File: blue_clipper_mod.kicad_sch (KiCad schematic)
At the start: 8 parts

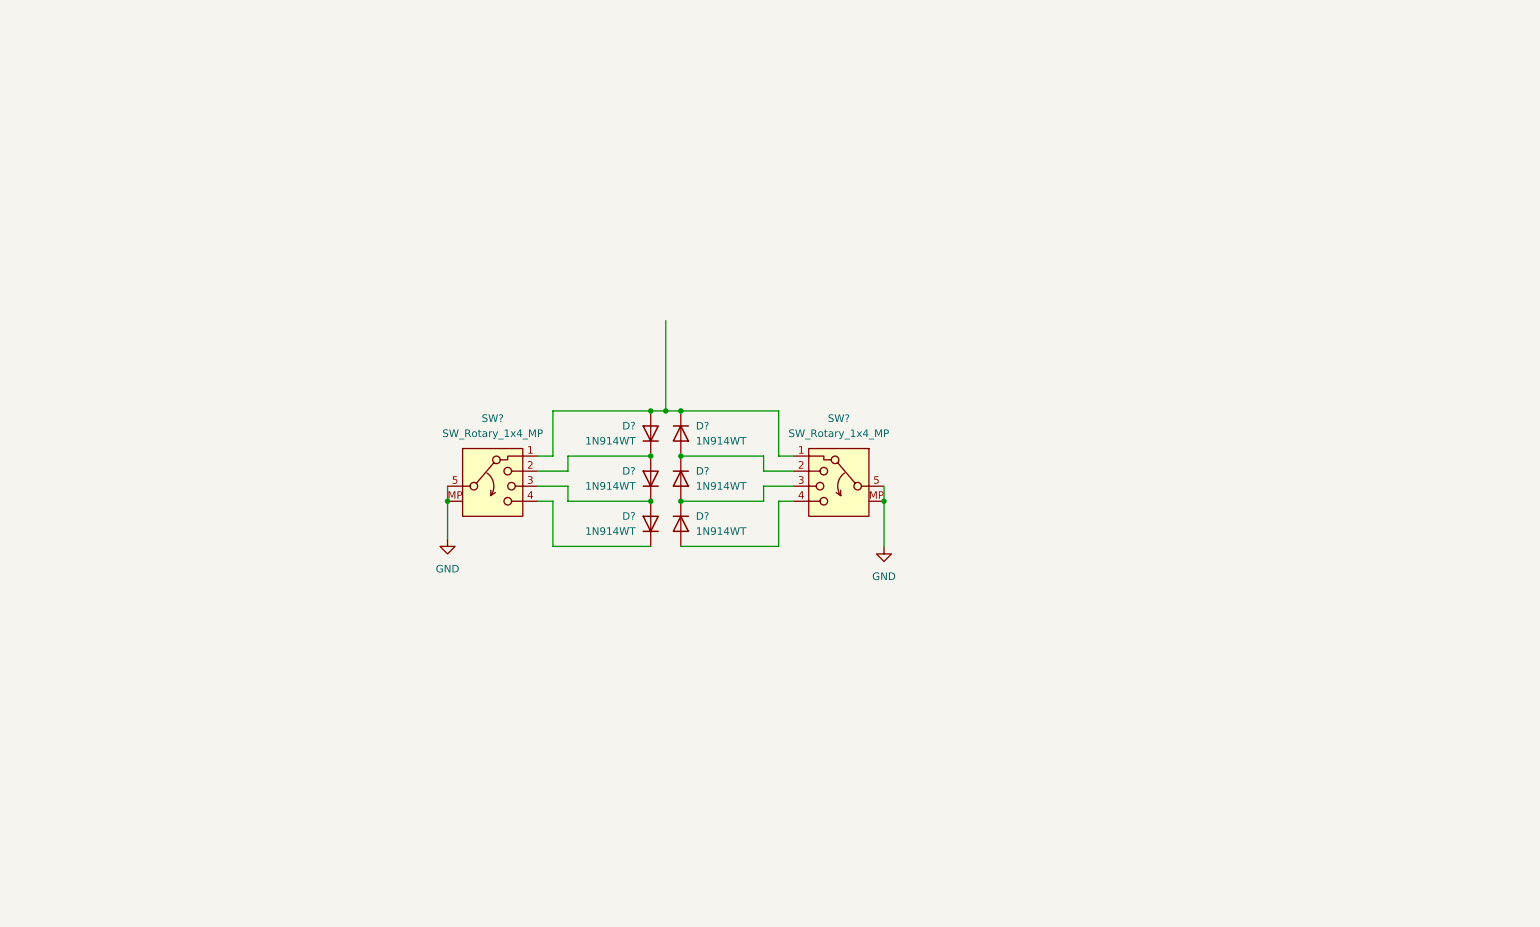
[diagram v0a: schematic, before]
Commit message: Clean Up schematic
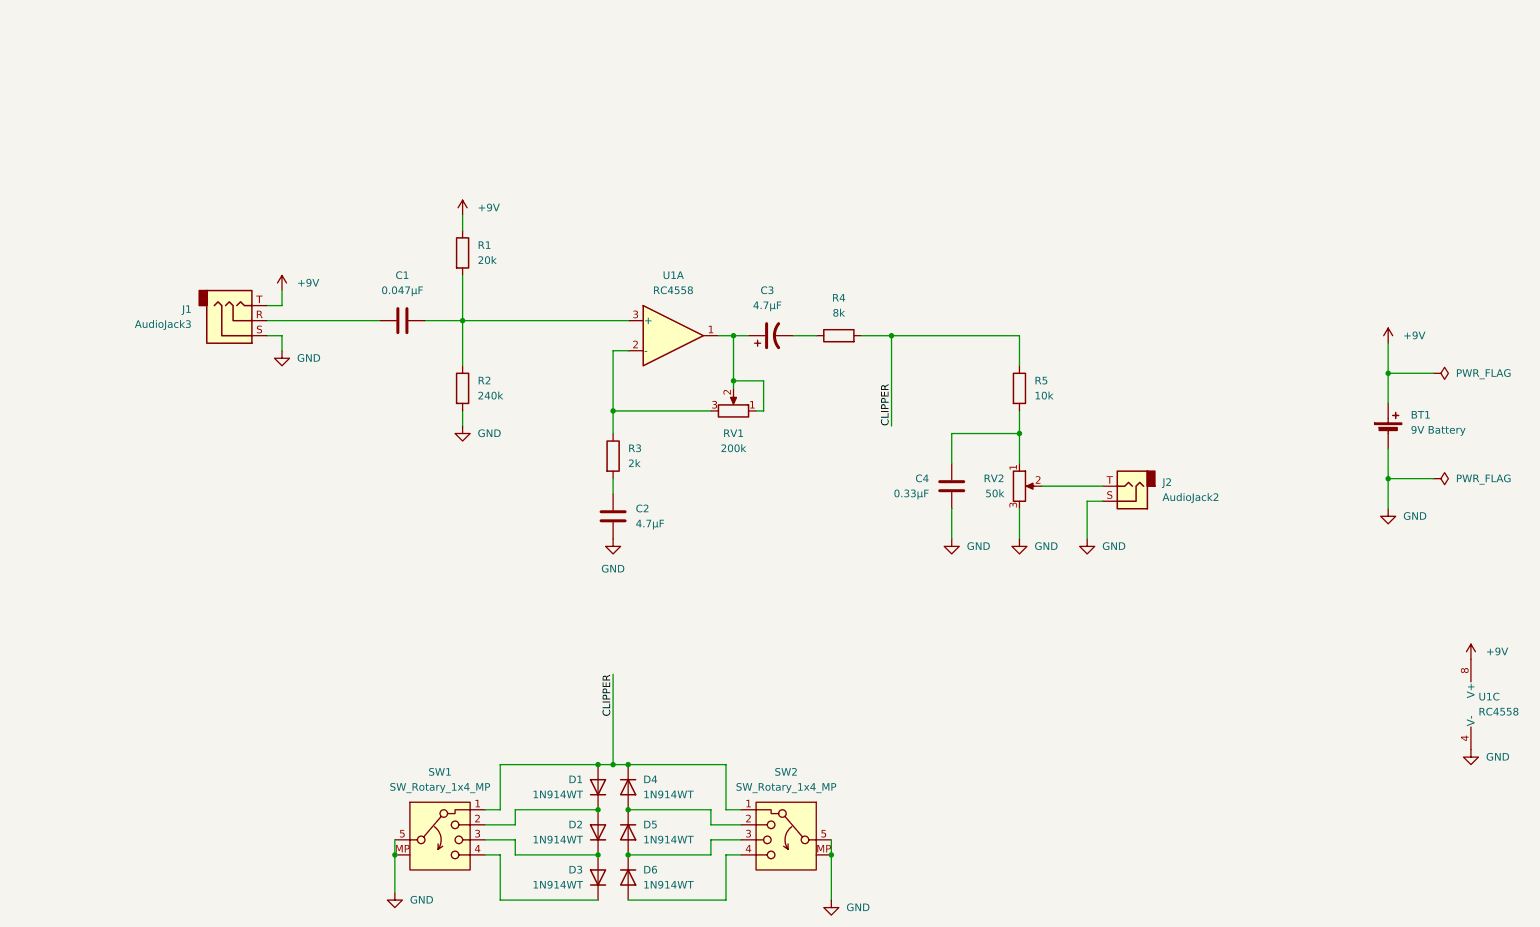
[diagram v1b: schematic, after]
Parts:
- added BT1: 9V Battery, symbol Device:Battery_Cell
- added C1: 0.047µF, symbol Device:C
- added C2: 4.7µF, symbol Device:C
- added C3: 4.7µF, symbol Device:C_Polarized_US
- added C4: 0.33µF, symbol Device:C
- added J1: AudioJack3, symbol Connector_Audio:AudioJack3
- added J2: AudioJack2, symbol Connector_Audio:AudioJack2
- added R1: 20k, symbol Device:R
- added R2: 240k, symbol Device:R
- added R3: 2k, symbol Device:R
- added R4: 8k, symbol Device:R
- added R5: 10k, symbol Device:R
- added RV1: 200k, symbol Device:R_Potentiometer
- added RV2: 50k, symbol Device:R_Potentiometer
- added U1: RC4558, symbol Amplifier_Operational:RC4558
- gave numbers to parts that had none: 8
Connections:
- net GND: now also BT1.2 (-), C2.2, C4.2, J1.S, J2.S, R2.2, RV2.3, U1.4 (V-)
- net CLIPPER: now reaches D1.2 (A), D4.1 (K), SW1.1, SW2.1
- net CLIPPER: now also R4.2, R5.1
- new net: C1.2, R1.2, R2.1, U1.3 (+)
- new net: C4.1, R5.2, RV2.1
- new net: J2.T, RV2.2
- new net: C3.1, RV1.1, RV1.2, U1.1
- new net: R3.1, RV1.3, U1.2 (-)
- new net: C2.1, R3.2
- new net: C3.2, R4.1
- new net: C1.1, J1.R
- new net +9V: BT1.1 (+), J1.T, R1.1, U1.8 (V+)
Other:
- moved on the sheet: D1, D2, D3, D4, D5, D6, SW1, SW2

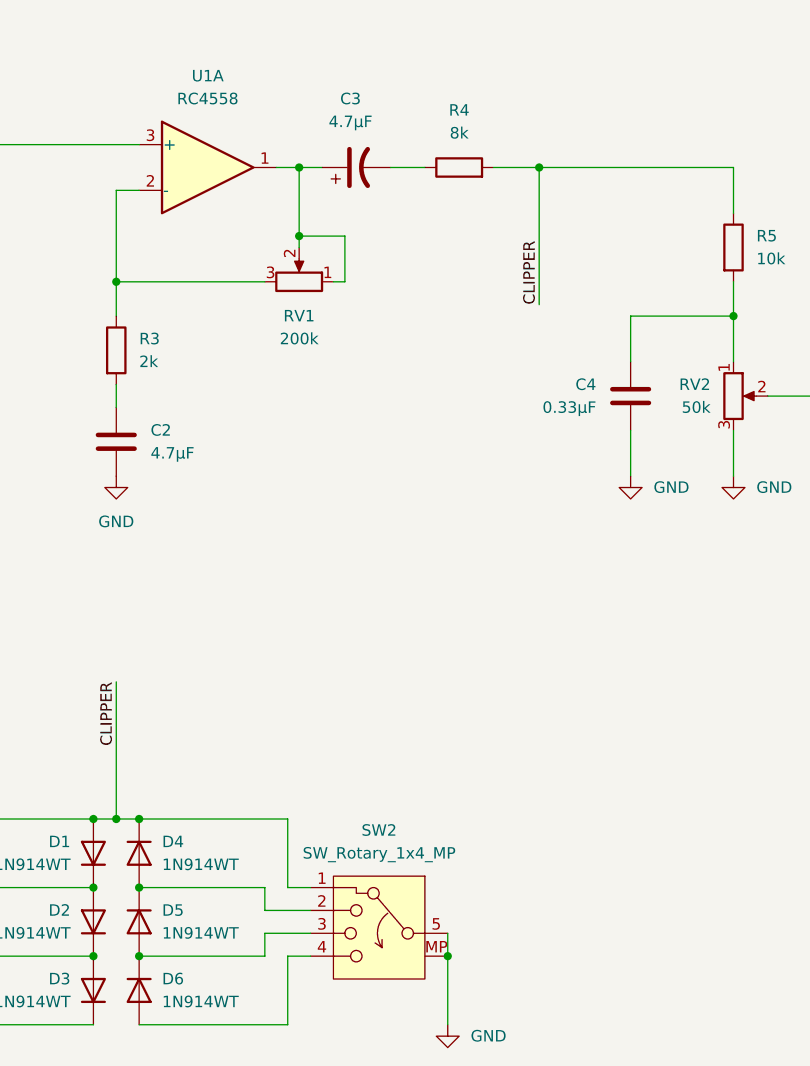
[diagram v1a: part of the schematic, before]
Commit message: schematic probably good - round tracks fully necessary
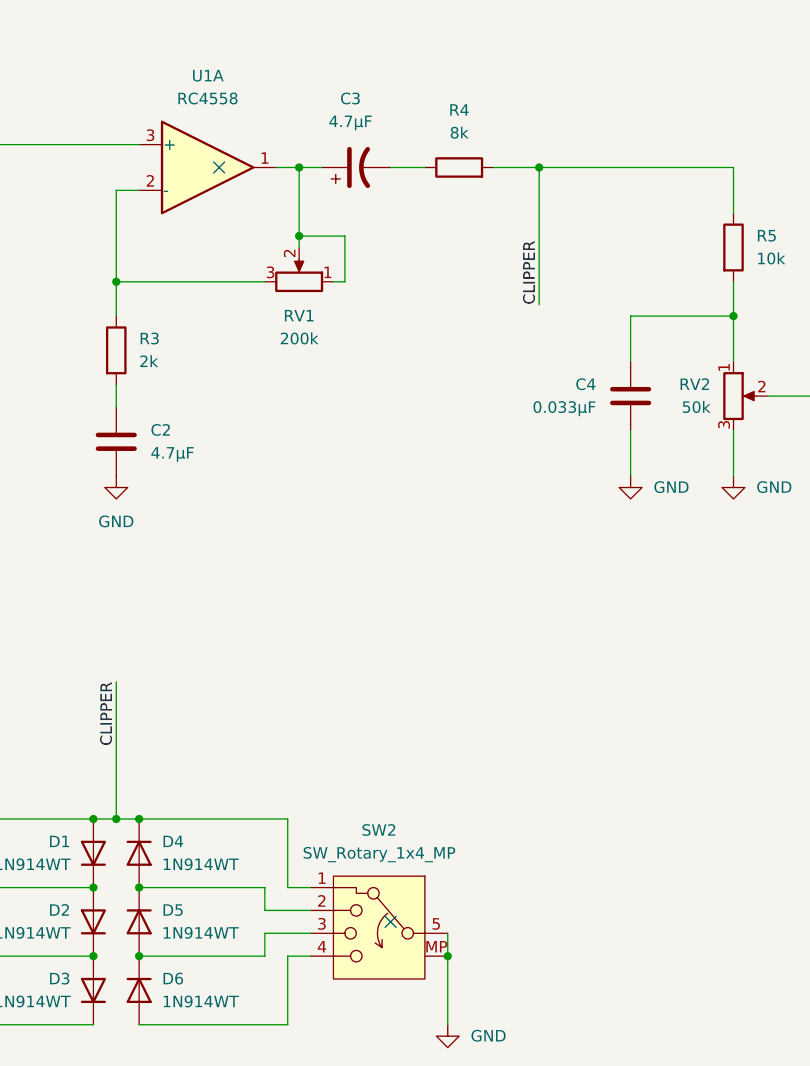
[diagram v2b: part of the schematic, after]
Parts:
- BT1: footprint (none) -> Battery:BatteryHolder_MPD_BA9VPC_1xPP3
- C1: footprint (none) -> Capacitor_THT:CP_Radial_Tantal_D6.0mm_P5.00mm
- C2: footprint (none) -> Capacitor_THT:CP_Radial_D22.0mm_P10.00mm_SnapIn
- C3: footprint (none) -> Capacitor_THT:CP_Radial_D26.0mm_P10.00mm_SnapIn
- C4: value 0.33µF -> 0.033µF; footprint (none) -> Capacitor_THT:C_Disc_D8.0mm_W5.0mm_P10.00mm
- J1, J2: footprint (none) -> Connector_Audio:Jack_3.5mm_CUI_SJ-3523-SMT_Horizontal
- R1, R2, R3, R4, R5: footprint (none) -> Resistor_THT:R_Axial_DIN0614_L14.3mm_D5.7mm_P5.08mm_Vertical
- RV1, RV2: footprint (none) -> Potentiometer_THT:Potentiometer_Piher_PC-16_Single_Vertical
- SW1, SW2: footprint (none) -> Rotary_Encoder:RotaryEncoder_Alps_EC12E-Switch_Vertical_H20mm_CircularMountingHoles
- U1: footprint (none) -> Package_DIP:DIP-8_W10.16mm
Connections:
- no-connect marks 0 -> 2
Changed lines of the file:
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@@
   (junction (at 193.04 100.33) (diameter 0) (color 0 0 0 0)
   )
+  (no_connect (at 135.89 83.82))
+  (no_connect (at 154.94 167.64))
   (wire (pts (xy 124.46 96.52) (xy 124.46 100.33))
     (stroke (width 0) (type default))
@@
       (effects (font (size 1.27 1.27)) (justify left))
     )
-    (property "Footprint" "" (at 97.282 69.85 90)
+    (property "Footprint" "Resistor_THT:R_Axial_DIN0614_L14.3mm_D5.7mm_P5.08mm_Vertical" (at 97.282 69.85 90)
       (effects (font (size 1.27 1.27)) hide)
     )
@@
       (effects (font (size 1.27 1.27)))
     )
-    (property "Footprint" "" (at 95.25 179.07 0)
+    (property "Footprint" "Rotary_Encoder:RotaryEncoder_Alps_EC12E-Switch_Vertical_H20mm_CircularMountingHoles" (at 95.25 179.07 0)
       (effects (font (size 1.27 1.27)) hide)
     )
@@
       (effects (font (size 1.27 1.27)) (justify right))
     )
-    (property "Footprint" "" (at 193.04 109.22 0)
+    (property "Footprint" "Potentiometer_THT:Potentiometer_Piher_PC-16_Single_Vertical" (at 193.04 109.22 0)
       (effects (font (size 1.27 1.27)) hide)
     )
@@
       (effects (font (size 1.27 1.27)) (justify right))
     )
-    (property "Value" "0.33µF" (at 177.8 110.49 0)
+    (property "Value" "0.033µF" (at 177.8 110.49 0)
       (effects (font (size 1.27 1.27)) (justify right))
     )
-    (property "Footprint" "" (at 182.5752 113.03 0)
+    (property "Footprint" "Capacitor_THT:C_Disc_D8.0mm_W5.0mm_P10.00mm" (at 182.5752 113.03 0)
       (effects (font (size 1.27 1.27)) hide)
     )
@@
       (effects (font (size 1.27 1.27)) (justify left))
     )
-    (property "Footprint" "" (at 191.262 92.71 90)
+    (property "Footprint" "Resistor_THT:R_Axial_DIN0614_L14.3mm_D5.7mm_P5.08mm_Vertical" (at 191.262 92.71 90)
       (effects (font (size 1.27 1.27)) hide)
     )
@@
       (effects (font (size 1.27 1.27)))
     )
-    (property "Footprint" "" (at 144.78 96.52 0)
+    (property "Footprint" "Potentiometer_THT:Potentiometer_Piher_PC-16_Single_Vertical" (at 144.78 96.52 0)
       (effects (font (size 1.27 1.27)) hide)
     )
@@
       (effects (font (size 1.27 1.27)) (justify left))
     )
-    (property "Footprint" "" (at 122.682 104.14 90)
+    (property "Footprint" "Resistor_THT:R_Axial_DIN0614_L14.3mm_D5.7mm_P5.08mm_Vertical" (at 122.682 104.14 90)
       (effects (font (size 1.27 1.27)) hide)
     )
@@
       (effects (font (size 1.27 1.27)))
     )
-    (property "Footprint" "" (at 134.62 83.82 0)
+    (property "Footprint" "Package_DIP:DIP-8_W10.16mm" (at 134.62 83.82 0)
       (effects (font (size 1.27 1.27)) hide)
     )
@@
       (effects (font (size 1.27 1.27)) (justify left))
     )
-    (property "Footprint" "" (at 125.4252 118.11 0)
+    (property "Footprint" "Capacitor_THT:CP_Radial_D22.0mm_P10.00mm_SnapIn" (at 125.4252 118.11 0)
       (effects (font (size 1.27 1.27)) hide)
     )
@@
       (effects (font (size 1.27 1.27)))
     )
-    (property "Footprint" "" (at 162.56 85.598 90)
+    (property "Footprint" "Resistor_THT:R_Axial_DIN0614_L14.3mm_D5.7mm_P5.08mm_Vertical" (at 162.56 85.598 90)
       (effects (font (size 1.27 1.27)) hide)
     )
@@
       (effects (font (size 1.27 1.27)) (justify left))
     )
-    (property "Footprint" "" (at 271.78 146.05 0)
+    (property "Footprint" "Package_DIP:DIP-8_W10.16mm" (at 271.78 146.05 0)
       (effects (font (size 1.27 1.27)) hide)
     )
@@
       (effects (font (size 1.27 1.27)))
     )
-    (property "Footprint" "" (at 153.67 179.07 0)
+    (property "Footprint" "Rotary_Encoder:RotaryEncoder_Alps_EC12E-Switch_Vertical_H20mm_CircularMountingHoles" (at 153.67 179.07 0)
       (effects (font (size 1.27 1.27)) hide)
     )
@@
       (effects (font (size 1.27 1.27)) (justify left))
     )
-    (property "Footprint" "" (at 255.27 98.806 90)
+    (property "Footprint" "Battery:BatteryHolder_MPD_BA9VPC_1xPP3" (at 255.27 98.806 90)
       (effects (font (size 1.27 1.27)) hide)
     )
@@
       (effects (font (size 1.27 1.27)) (justify right))
     )
-    (property "Footprint" "" (at 212.09 109.22 0)
+    (property "Footprint" "Connector_Audio:Jack_3.5mm_CUI_SJ-3523-SMT_Horizontal" (at 212.09 109.22 0)
       (effects (font (size 1.27 1.27)) hide)
     )
@@
       (effects (font (size 1.27 1.27)) (justify left))
     )
-    (property "Footprint" "" (at 97.282 92.71 90)
+    (property "Footprint" "Resistor_THT:R_Axial_DIN0614_L14.3mm_D5.7mm_P5.08mm_Vertical" (at 97.282 92.71 90)
       (effects (font (size 1.27 1.27)) hide)
     )
@@
       (effects (font (size 1.27 1.27)) (justify right))
     )
-    (property "Footprint" "" (at 60.96 81.28 0)
+    (property "Footprint" "Connector_Audio:Jack_3.5mm_CUI_SJ-3523-SMT_Horizontal" (at 60.96 81.28 0)
       (effects (font (size 1.27 1.27)) hide)
     )
@@
       (effects (font (size 1.27 1.27)))
     )
-    (property "Footprint" "" (at 92.71 80.3148 0)
+    (property "Footprint" "Capacitor_THT:CP_Radial_Tantal_D6.0mm_P5.00mm" (at 92.71 80.3148 0)
       (effects (font (size 1.27 1.27)) hide)
     )
@@
       (effects (font (size 1.27 1.27)))
     )
-    (property "Footprint" "" (at 151.13 83.82 0)
-      (effects (font (size 1.27 1.27)) hide)
-    )
+    (property "Footprint" "Capacitor_THT:CP_Radial_D26.0mm_P10.00mm_SnapIn" (at 151.13 83.82 0)
+      (effects (font (size 1.27 1.27)) hide)
+    )

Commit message: fix everything
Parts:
- removed C3: 4.7µF, Capacitor_THT:CP_Radial_D26.0mm_P10.00mm_SnapIn, symbol Device:C_Polarized_US
- removed J1: AudioJack3, Connector_Audio:Jack_3.5mm_CUI_SJ-3523-SMT_Horizontal, symbol Connector_Audio:AudioJack3
- removed J2: AudioJack2, Connector_Audio:Jack_3.5mm_CUI_SJ-3523-SMT_Horizontal, symbol Connector_Audio:AudioJack2
- removed SW1, SW2: SW_Rotary_1x4_MP, Rotary_Encoder:RotaryEncoder_Alps_EC12E-Switch_Vertical_H20mm_CircularMountingHoles, symbol Switch:SW_Rotary_1x4_MP
- added C3: 4.7µF, Capacitor_THT:CP_Radial_D4.0mm_P1.50mm, symbol Device:C
- added H1, H2, H3, H4: MountingHole, MountingHole:MountingHole_3.2mm_M3, symbol Mechanical:MountingHole
- added J1: IN, custom:jack_pads, symbol Connector_Audio:AudioJack2_SwitchT
- added J2: OUT, custom:jack_pads, symbol Connector_Audio:AudioJack2_SwitchT
- added JP1, JP2: SolderJumper_2_Open, Jumper:SolderJumper-2_P1.3mm_Open_RoundedPad1.0x1.5mm, symbol Jumper:SolderJumper_2_Open
- added R6, R7: 50k, Resistor_SMD:R_0603_1608Metric_Pad0.98x0.95mm_HandSolder, symbol Device:R
- added SW1, SW2: ~, Connector_PinHeader_2.54mm:PinHeader_1x05_P2.54mm_Vertical, symbol custom:SP4T
- added SW3: BYPASS, Connector_PinHeader_2.54mm:PinHeader_1x06_P2.54mm_Vertical, symbol Switch:SW_Push_DPDT
- added unit 2 of U1
- BT1: footprint Battery:BatteryHolder_MPD_BA9VPC_1xPP3 -> Connector_PinHeader_2.54mm:PinHeader_1x02_P2.54mm_Vertical
- C1: footprint Capacitor_THT:CP_Radial_Tantal_D6.0mm_P5.00mm -> Capacitor_SMD:C_0603_1608Metric
- C2: footprint Capacitor_THT:CP_Radial_D22.0mm_P10.00mm_SnapIn -> Capacitor_THT:CP_Radial_D4.0mm_P1.50mm
- C4: footprint Capacitor_THT:C_Disc_D8.0mm_W5.0mm_P10.00mm -> Capacitor_SMD:C_0603_1608Metric_Pad1.08x0.95mm_HandSolder
- D1, D2, D3, D4, D5, D6: symbol Diode:1N914WT -> Diode:1N4148WT
- R1, R3, R4, R5: footprint Resistor_THT:R_Axial_DIN0614_L14.3mm_D5.7mm_P5.08mm_Vertical -> Resistor_SMD:R_0603_1608Metric_Pad0.98x0.95mm_HandSolder
- R2: value 240k -> 20k; footprint Resistor_THT:R_Axial_DIN0614_L14.3mm_D5.7mm_P5.08mm_Vertical -> Resistor_SMD:R_0603_1608Metric_Pad0.98x0.95mm_HandSolder
- RV1: value 200k -> 100k; footprint Potentiometer_THT:Potentiometer_Piher_PC-16_Single_Vertical -> Connector_PinHeader_2.54mm:PinHeader_1x03_P2.54mm_Vertical
- RV2: footprint Potentiometer_THT:Potentiometer_Piher_PC-16_Single_Vertical -> Connector_PinHeader_2.54mm:PinHeader_1x03_P2.54mm_Vertical
- U1: footprint Package_DIP:DIP-8_W10.16mm -> Package_DIP:DIP-8_W7.62mm_Socket
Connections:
- net GND: now also J1.S, J1.TN, J2.S, J2.TN, SW1.1, SW2.1, SW3.6 (C), U1.5 (+), U1.6 (-)
- net at D1.1 (K), D2.2 (A): now also SW1.4
- net at D2.1 (K), D3.2 (A): now also SW1.3
- net at D3.1 (K): now also SW1.2
- net EFFECT_OUT: now reaches RV2.2
- net EFFECT_OUT: now also SW3.1 (A)
- net at D4.2 (A), D5.1 (K): now also SW2.4
- net at D5.2 (A), D6.1 (K): now also SW2.3
- net at RV1.1, RV1.2: now also JP2.1 (A), R7.1; no longer U1.1
- net at R3.1, U1.2 (-): now also JP1.1 (A), R6.1; no longer RV1.3
- net at D6.2 (A): now also SW2.2
- net at R4.1: now also C3.2
- net EFFECT_IN: now reaches C1.1
- net EFFECT_IN: now also SW3.5 (B)
- new net: C3.1, JP2.2 (B), R7.2, U1.1
- new net: JP1.2 (B), R6.2, RV1.3
- new net IN: J1.T, SW3.3 (C), SW3.4 (A)
- new net OUT: J2.T, SW3.2 (B)
- no-connect marks 2 -> 3
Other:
- moved on the sheet: BT1, C1, C2, C4, D1, D2, D3, D4, D5, D6, R1, R2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
